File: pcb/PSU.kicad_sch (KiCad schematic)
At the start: 45 parts

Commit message: PartNumber update
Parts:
- C21, C22, C30, C31, C34, C36, C43, C47, C48, C67: Manufacturer_Part_Number (none) -> CL31B106KBHNNNE
- C23, C24, C26, C28, C32, C33, C37, C38, C41, C42, C45, C46, C68, C69, C70, C71: Manufacturer_Part_Number (none) -> GRM188R71H104KA93D
- D10: Manufacturer_Part_Number (none) -> ESD5Z3.3T1G
- D12: Manufacturer_Part_Number (none) -> SMF5.0CA
- F1, F2, F3, F4: Manufacturer_Part_Number (none) -> SN020-30
- L1, L2, L3, L4: Manufacturer_Part_Number (none) -> LQH32PN101MN0L

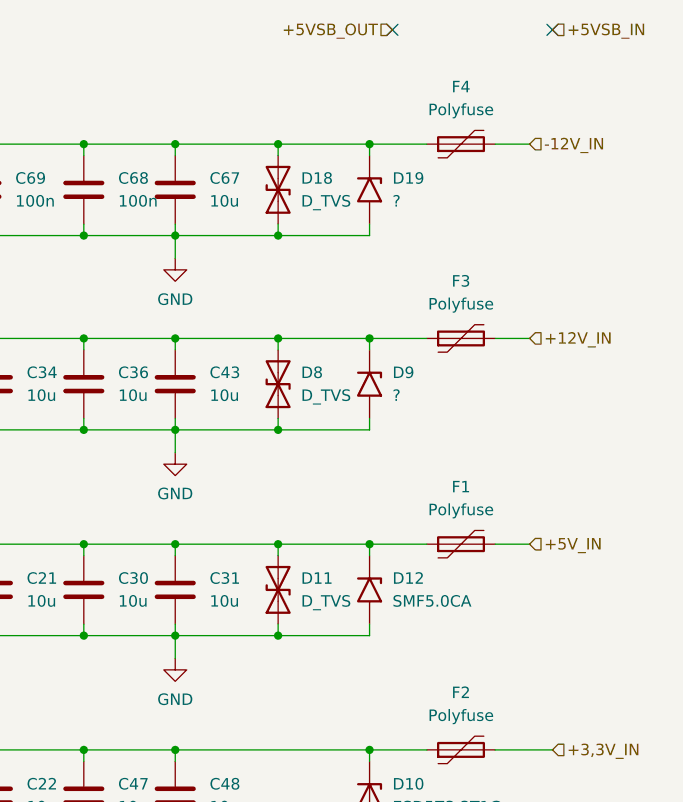
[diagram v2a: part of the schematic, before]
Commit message: Unify component values/footprints per checklist; add via-in-pad DRC rule; regenerate production outputs
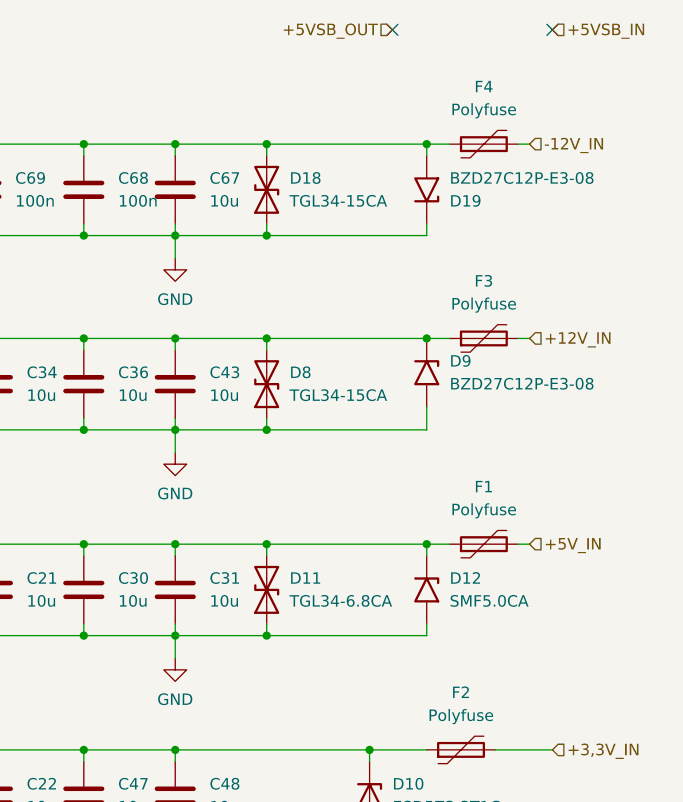
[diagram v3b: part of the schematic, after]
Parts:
- C21, C22, C30, C31, C34, C36, C43, C47, C48, C67: footprint Capacitor_SMD:C_1206_3216Metric_Pad1.33x1.80mm_HandSolder -> Capacitor_SMD:C_1206_3216Metric
- C23, C24, C26, C28, C32, C33, C37, C38, C41, C42, C45, C46, C68, C69, C70, C71: footprint Capacitor_SMD:C_0603_1608Metric_Pad1.08x0.95mm_HandSolder -> Capacitor_SMD:C_0603_1608Metric
- D11: value D_TVS -> TGL34-6.8CA; Manufacturer_Part_Number (none) -> TGL34-6.8CA
- D18, D8: value D_TVS -> TGL34-15CA; Manufacturer_Part_Number (none) -> TGL34-15CA
- D19, D9: value ? -> BZD27C12P-E3-08; Manufacturer_Part_Number (none) -> BZD27C12P-E3-08
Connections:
- net GND: now also D19.1 (A1); no longer D19.2 (A2)
- net at C67.1, C68.1, C69.1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: now also D19.2 (A2); no longer D19.1 (A1)
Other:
- moved on the sheet: D11, D12, D18, D19, D8, D9, F1, F3, F4
